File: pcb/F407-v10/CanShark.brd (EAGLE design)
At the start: 97 x 80 mm, 132 parts, among them IC1 STM32F407V, IC2 KSZ8051MLL, K2 JACK_POWER_2,1, U1 SN65HVD230DR, U2 SN65HVD230DR, U3 LM2594M-ADJ, U4 LM2594M-ADJ, U5 TSH24IDT, U6 MCP602-E/SN

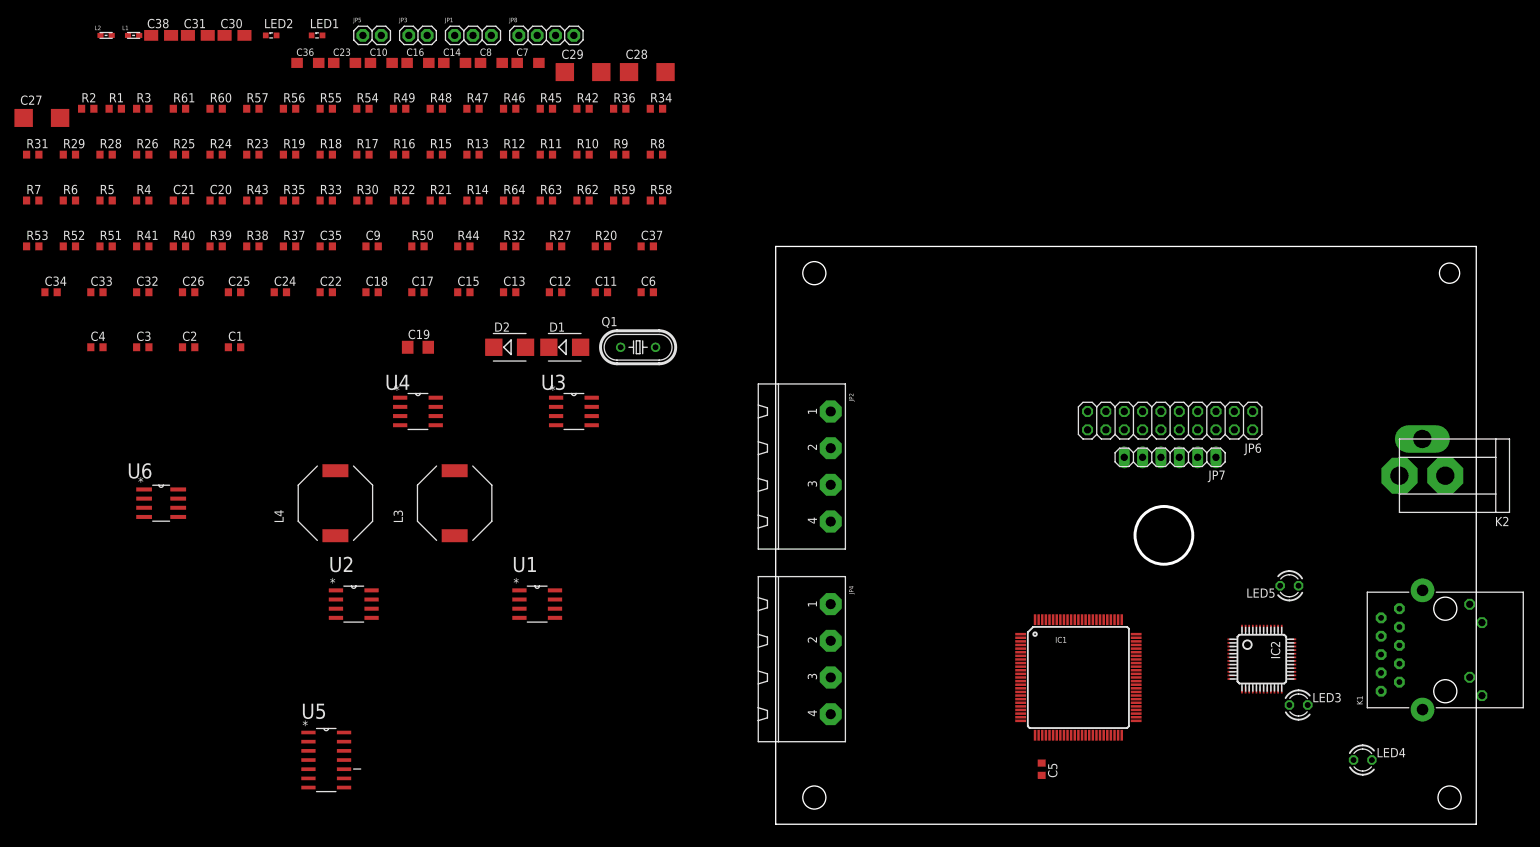
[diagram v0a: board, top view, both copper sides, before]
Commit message: Add MCU crystal to schematic, change pcb
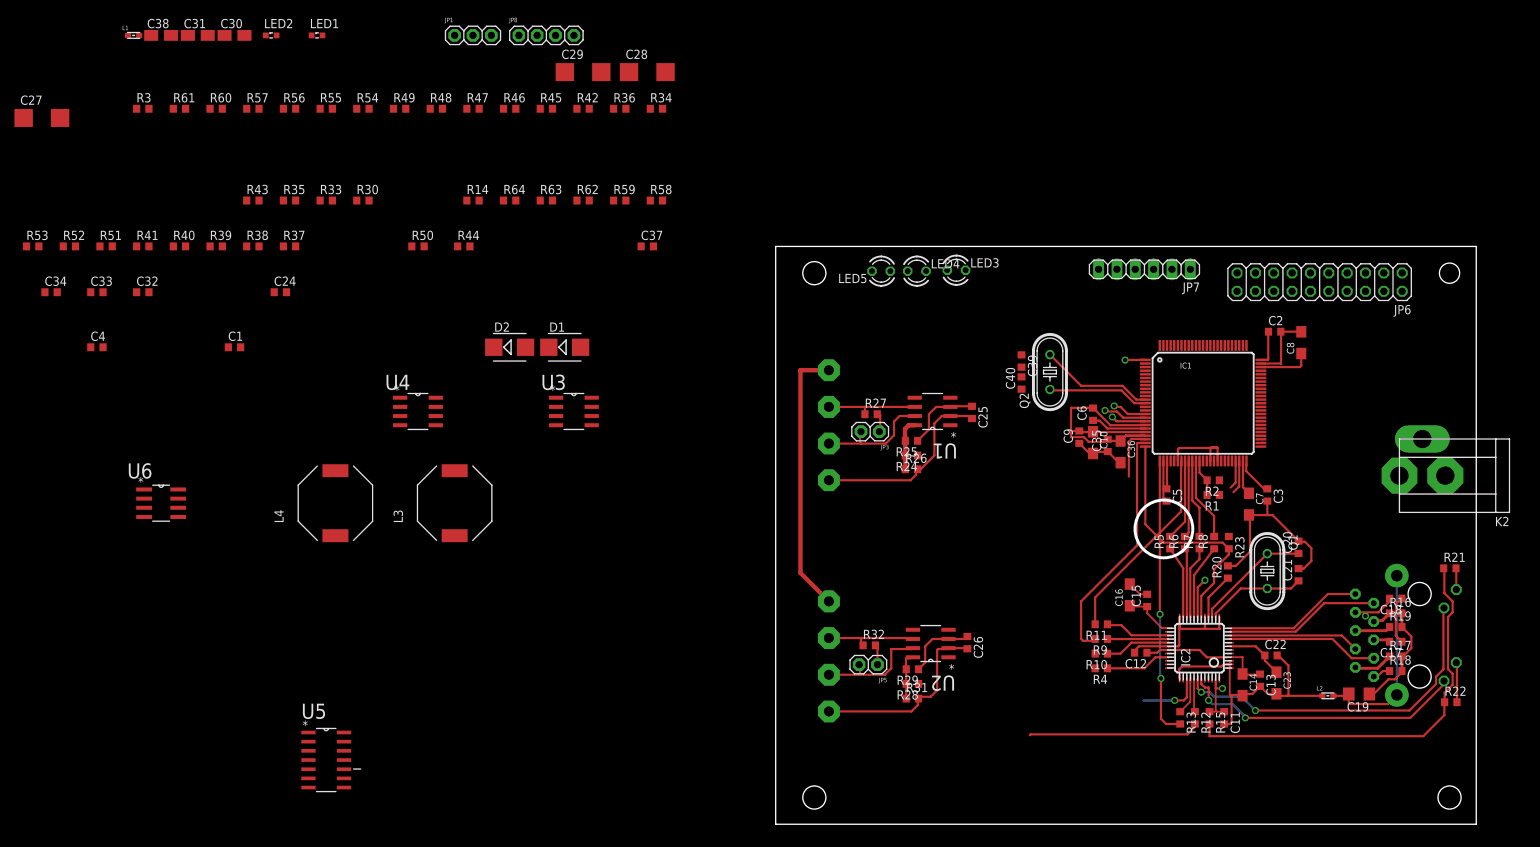
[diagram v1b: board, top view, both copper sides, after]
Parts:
- added C39, C40: 22p, #Kondenzatory:SMD0603
- added Q2: (no value), crystal:HC49U-V
- moved L2 192.3 mm to (76.5, 17.8)
- moved R7 168.3 mm to (58.7, 39.0), turned to 90 degrees
- moved R19 166.5 mm to (85.9, 27.3)
- moved R18 164.4 mm to (85.9, 21.2)
- moved R2 164.1 mm to (60.6, 47.6), turned to 180 degrees
- moved C21 163.4 mm to (72.4, 34.5), turned to 90 degrees
- moved R6 161.5 mm to (56.6, 39.0), turned to 90 degrees
- moved R22 161.3 mm to (93.5, 16.9)
- moved R1 161.1 mm to (60.6, 45.6), turned to 180 degrees
- moved R17 159.0 mm to (85.9, 23.2)
- moved C20 157.4 mm to (72.4, 38.4), turned to 90 degrees
- moved C3 157.0 mm to (68.1, 45.6), turned to 270 degrees
- moved C23 155.0 mm to (69.3, 19.6), turned to 270 degrees
- moved R5 154.7 mm to (54.6, 39.0), turned to 90 degrees
- moved R16 151.8 mm to (85.9, 29.2)
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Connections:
- new net OSC_IN: C39.1, IC1.12, Q2.2
- new net OSC_OUT: C40.1, IC1.13, Q2.1
- net CAN1_H: now also JP2.2; no longer JP2.3
- net CAN1_L: now also JP2.3; no longer JP2.2
- net CANL: now also JP4.3; no longer JP4.2
- net ETH_MDC: no longer R23.2
- net ETH_MDIO: now also R23.2
- net EXTSUPPLY: now also JP2.4, JP4.4; no longer JP2.1, JP4.1
- net GND: now also C39.2, C40.2, JP2.1, JP4.1; no longer JP2.4, JP4.4
- net N$14: now also JP4.2; no longer JP4.3
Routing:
- net GND: track 0.00 -> 179.4 mm
- net +3V3: track 0.00 -> 137.0 mm
- net N$50: track 0.00 -> 48.1 mm, vias 0 -> 2
- net N$51: track 0.00 -> 39.8 mm, vias 0 -> 2
- net ETH_MII_COL: track 0.00 -> 39.2 mm, vias 0 -> 2
- net EXTSUPPLY: track 0.00 -> 37.6 mm
- net ETH_MDIO: track 0.00 -> 34.8 mm
- net ETH_MII_RX_CLK: track 0.00 -> 33.6 mm
- net ETH_MII_CRS: track 0.00 -> 31.1 mm
- net ETH_MII_RX_DV: track 0.00 -> 27.6 mm
- net N$48: track 0.00 -> 27.3 mm
- net N$39: track 0.00 -> 21.5 mm
- net N$37: track 0.00 -> 21.0 mm
- net N$40: track 0.00 -> 19.3 mm
- net N$36: track 0.00 -> 19.2 mm
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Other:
- outline, holes or cut-outs redrawn

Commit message: Change Board
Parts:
- moved C4 137.7 mm to (43.7, 65.8), turned to 90 degrees
- moved R3 136.3 mm to (43.2, 60.7), turned to 180 degrees
- moved C1 127.8 mm to (52.8, 69.2)
- moved C24 112.8 mm to (43.2, 58.7), turned to 180 degrees
- moved JP1 104.9 mm to (56.1, 71.9)
- moved C37 65.1 mm to (45.7, 65.8), turned to 270 degrees
- moved C12 2.16 mm to (48.6, 22.7)
- moved C39 0.77 mm to (33.9, 64.9)
- moved C6 0.77 mm to (43.2, 56.6), turned to 0 degrees
- moved C40 0.77 mm to (33.9, 61.8)
- moved Q2 0.76 mm to (38.0, 63.4)
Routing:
- net ETH_MII_TXD0: track 0.00 -> 60.1 mm, vias 0 -> 1
- net ETH_MII_TXD1: track 0.27 -> 60.1 mm, vias 0 -> 1
- net ETH_INTRP: track 0.00 -> 57.9 mm, vias 0 -> 2
- net ETH_RST: track 8.89 -> 59.8 mm, vias 1 -> 2
- net ETH_MII_TX_CLK: track 4.82 -> 55.6 mm, vias 1 -> 2
- net ETH_MII_TXD3: track 11.6 -> 61.7 mm, vias 2 -> 1
- net ETH_MII_TXD2: track 6.00 -> 54.7 mm
- net ETH_MII_TX_EN: track 4.65 -> 51.6 mm, vias 0 -> 2
- net ETH_MII_CRS: track 31.1 -> 72.4 mm
- net GND: track 179.4 -> 219.5 mm, vias 0 -> 2
- net ETH_MDC: track 10.3 -> 49.2 mm, vias 2 -> 3
- net ETH_MII_RX_ER: track 3.97 -> 41.2 mm, vias 0 -> 2
- net +3V3: track 137.0 -> 165.6 mm
- net ETH_MII_COL: track 39.2 -> 18.0 mm
- net NRST: track 0.00 -> 9.55 mm
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
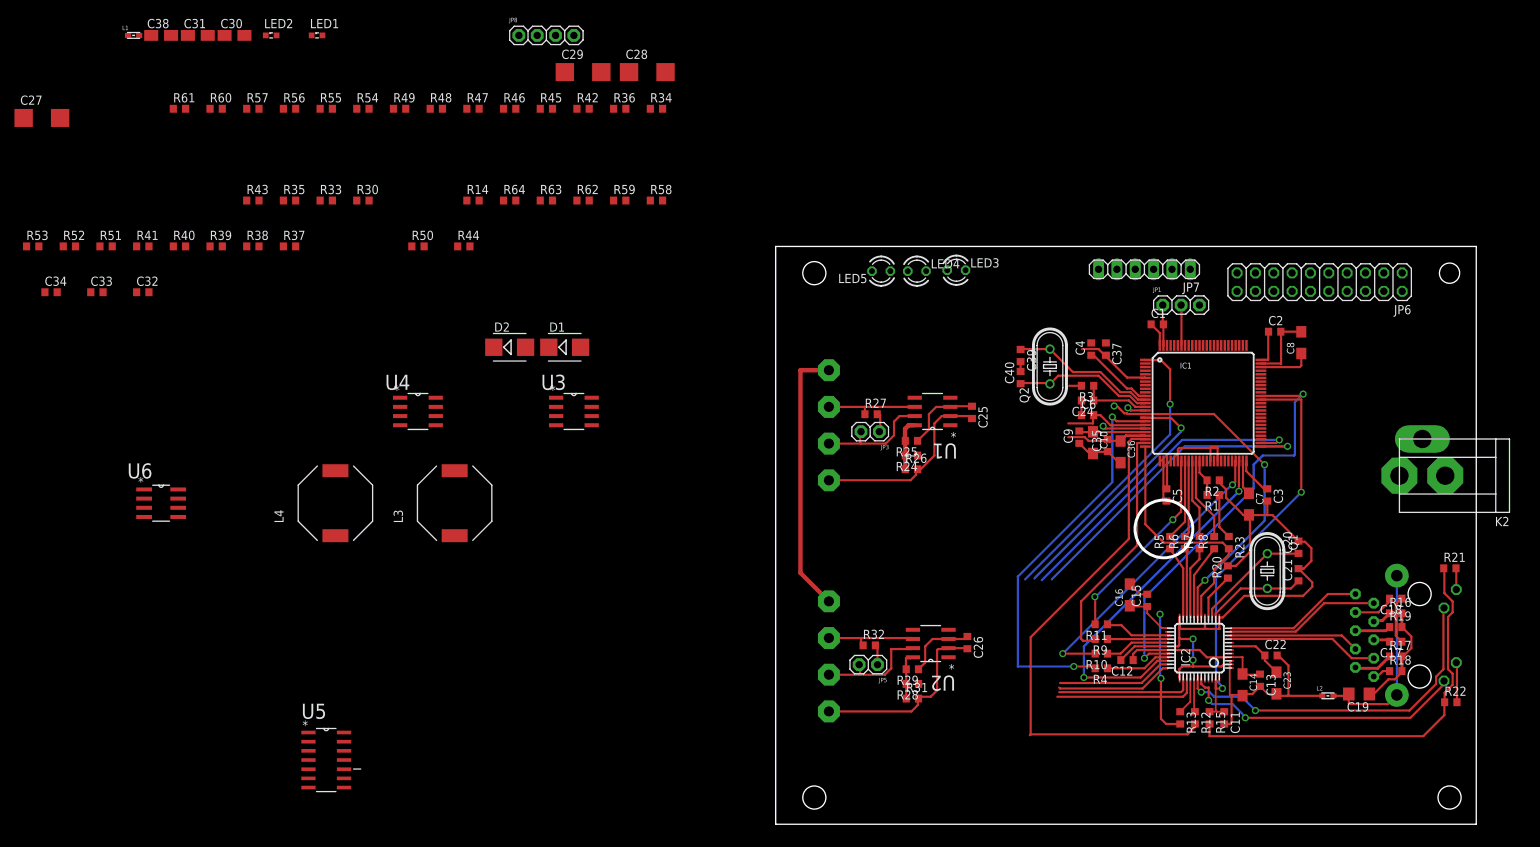
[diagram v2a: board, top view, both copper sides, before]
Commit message: design PCB modules
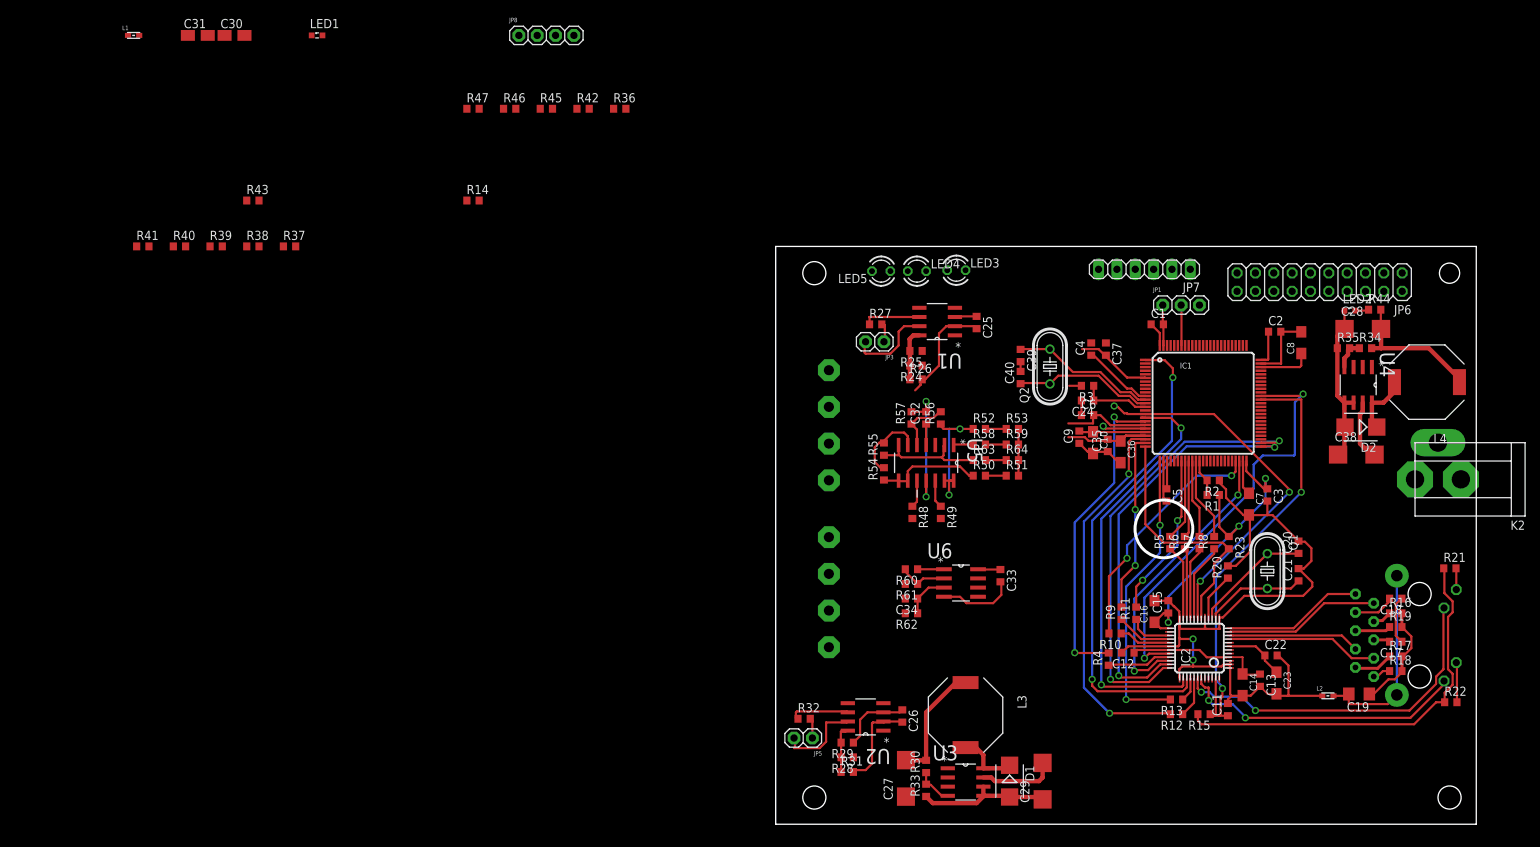
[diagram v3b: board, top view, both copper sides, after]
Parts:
- C38: device rcl:A/3216-18R -> rcl:C/6032-28R
- moved C38 175.4 mm to (80.4, 51.2)
- moved LED2 154.1 mm to (79.5, 71.1)
- moved L4 152.1 mm to (90.2, 61.2), turned to 90 degrees
- moved C27 150.6 mm to (18.0, 6.35), turned to 90 degrees
- moved R35 147.3 mm to (78.6, 65.9)
- moved R53 138.0 mm to (32.8, 54.7)
- moved C33 131.1 mm to (31.1, 34.4), turned to 270 degrees
- moved U4 130.2 mm to (80.6, 60.8), turned to 270 degrees
- moved R51 129.4 mm to (32.8, 48.3)
- moved R52 128.5 mm to (28.2, 54.7)
- moved C34 126.5 mm to (18.8, 31.2), turned to 180 degrees
- moved R44 126.4 mm to (82.9, 71.2)
- moved R61 120.8 mm to (18.8, 33.3), turned to 180 degrees
- moved D2 118.4 mm to (81.0, 55.0), turned to 180 degrees
- moved C29 117.0 mm to (37.0, 5.97), turned to 90 degrees
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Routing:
- net GND: track 219.5 -> 269.1 mm, vias 2 -> 4
- net +3V3: track 165.6 -> 204.1 mm, vias 0 -> 3
- net ETH_MII_COL: track 18.0 -> 41.1 mm
- net V+: track 0.00 -> 22.6 mm
- net ETH_MII_CRS: track 72.4 -> 52.6 mm, vias 0 -> 2
- net N$60: track 0.00 -> 19.4 mm, vias 0 -> 2
- net EXTSUPPLY: track 37.6 -> 19.1 mm
- net N$65: track 0.00 -> 15.9 mm
- net N$61: track 0.00 -> 14.6 mm
- net ETH_MII_TX_CLK: track 55.6 -> 44.4 mm
- net ETH_MII_TX_EN: track 51.6 -> 40.8 mm
- net N$66: track 0.00 -> 10.7 mm
- net ADC_TRIG: track 11.8 -> 2.87 mm
- net N$28: track 0.00 -> 8.78 mm
- net ETH_MII_RX_CLK: track 33.6 -> 24.9 mm, vias 0 -> 2
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
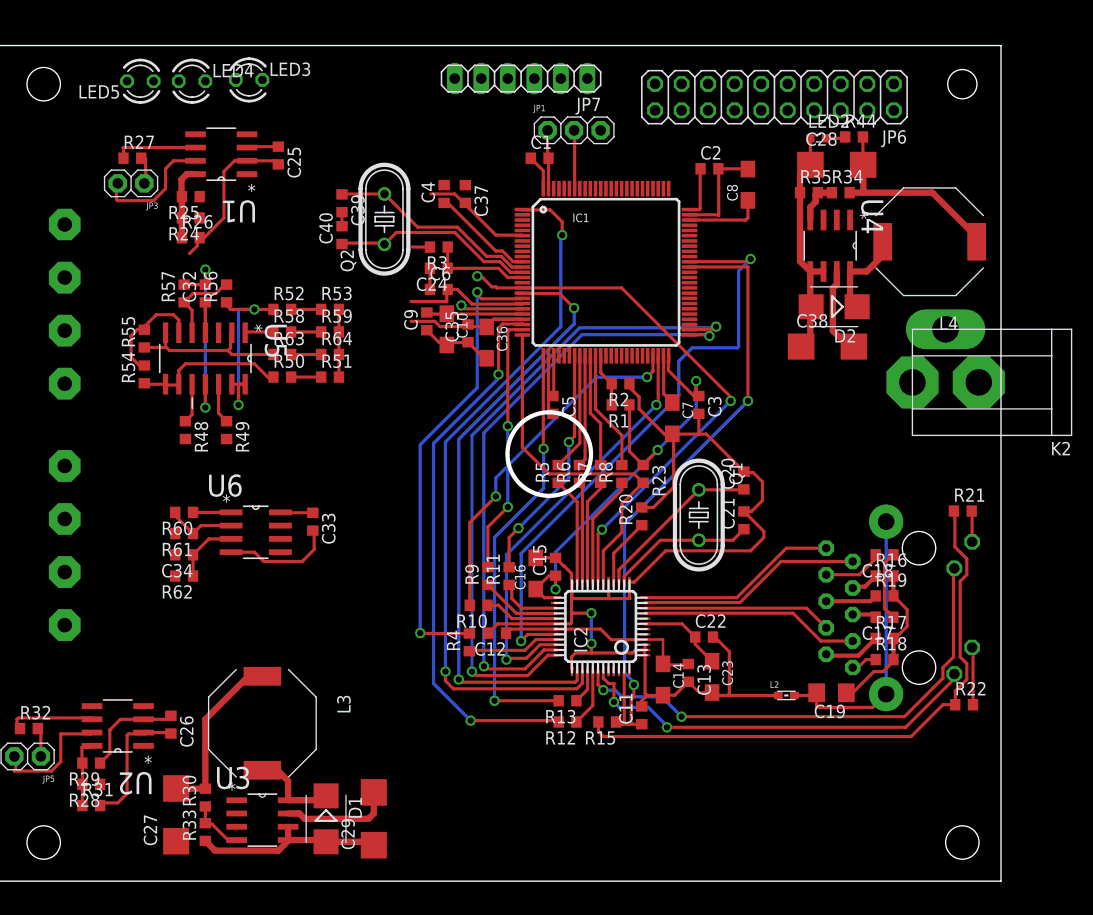
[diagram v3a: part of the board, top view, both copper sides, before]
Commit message: Rotate groups on board
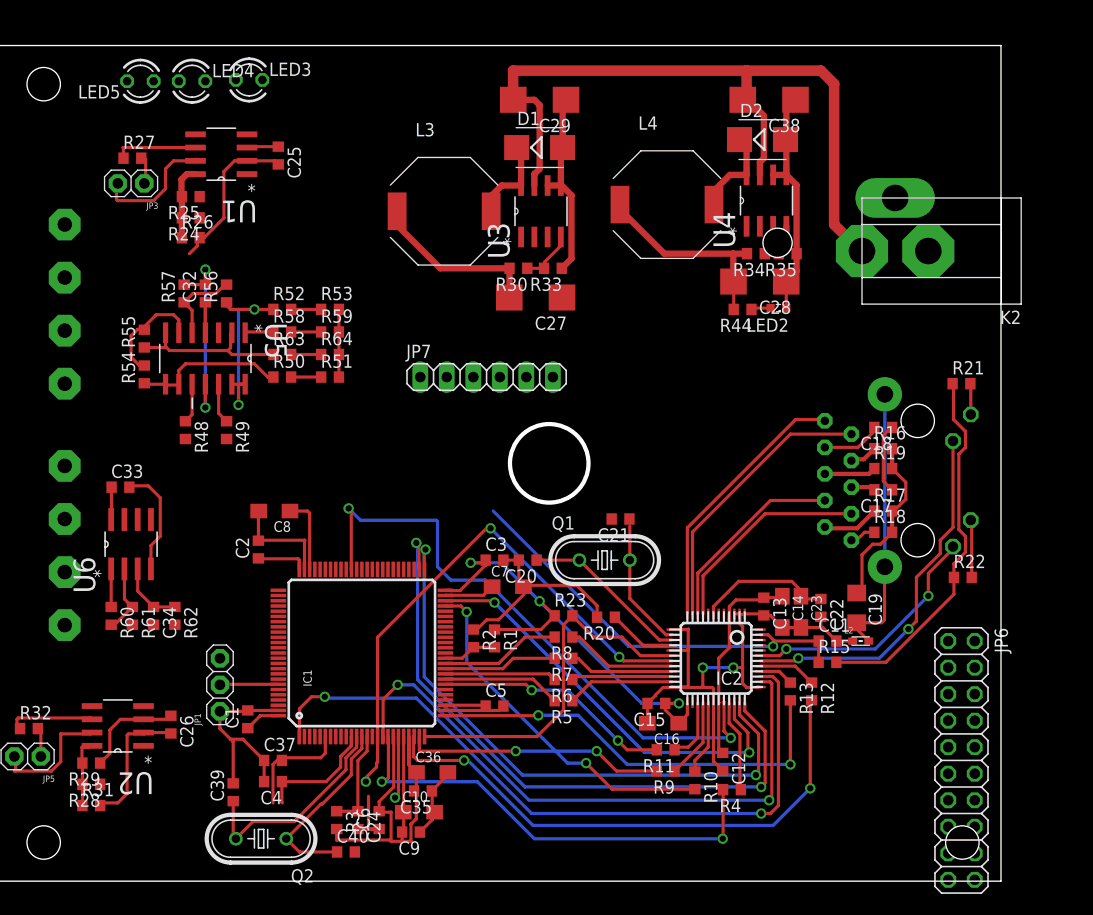
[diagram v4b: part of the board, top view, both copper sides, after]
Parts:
- moved C29 70.6 mm to (52.8, 74.8), turned to 180 degrees
- moved D1 67.4 mm to (52.8, 70.2), turned to 0 degrees
- moved JP6 66.0 mm to (93.2, 11.6), turned to 270 degrees
- moved U3 64.1 mm to (53.0, 64.1), turned to 90 degrees
- moved R33 63.4 mm to (54.1, 58.7), turned to 180 degrees
- moved JP1 63.0 mm to (22.2, 18.8), turned to 90 degrees
- moved C1 60.6 mm to (24.9, 15.5), turned to 90 degrees
- moved Q2 60.5 mm to (26.2, 4.06), turned to 180 degrees
- moved C27 60.3 mm to (52.5, 55.9), turned to 180 degrees
- moved C40 59.1 mm to (34.3, 2.79), turned to 0 degrees
- moved R30 58.9 mm to (50.8, 58.7), turned to 180 degrees
- moved C4 58.6 mm to (27.3, 9.53), turned to 180 degrees
- moved C39 57.3 mm to (23.5, 8.51), turned to 90 degrees
- moved C37 57.3 mm to (27.3, 11.6), turned to 0 degrees
- moved C2 56.5 mm to (25.9, 31.8), turned to 90 degrees
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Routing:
- net EXTSUPPLY: track 19.1 -> 73.5 mm
- net GND: track 269.1 -> 242.1 mm
- net ETH_RST: track 62.5 -> 40.6 mm, vias 2 -> 1
- net N$51: track 39.8 -> 24.1 mm
- net N$50: track 48.1 -> 35.2 mm
- net +3V3: track 204.1 -> 191.7 mm
- net N$40: track 19.3 -> 25.8 mm
- net N$39: track 21.5 -> 26.9 mm
- net N$9: track 8.31 -> 13.0 mm
- net N$55: track 13.9 -> 12.4 mm
- net OSC_OUT: track 19.5 -> 18.2 mm
- net N$38: track 18.1 -> 19.0 mm
- net N$37: track 21.0 -> 20.3 mm
- net N$48: track 27.3 -> 26.6 mm
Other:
- outline, holes or cut-outs redrawn
